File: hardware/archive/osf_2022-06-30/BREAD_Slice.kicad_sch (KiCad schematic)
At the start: 40 parts, among them J1 Conn_01x10_Female, J2 Term_2, J3 Term_2, J4 Term_2, J5 Term_2, J6 Term_2, J7 Term_2, J8 Term_2, K1 G5Q-1, Q1 STGP7NC60HD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

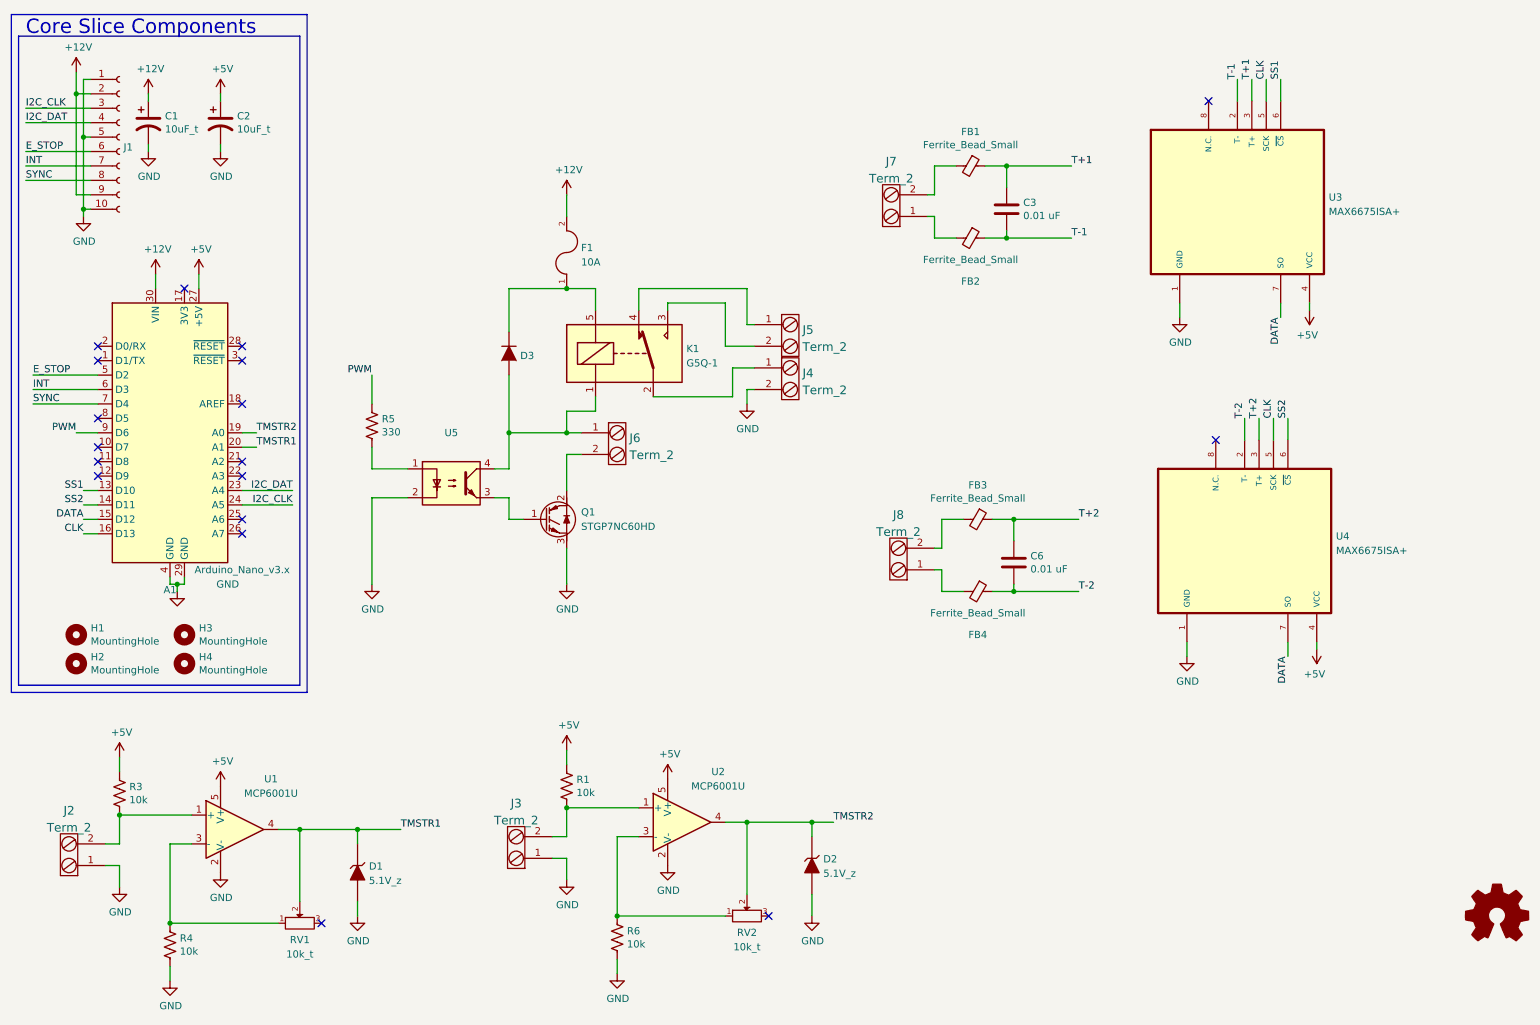
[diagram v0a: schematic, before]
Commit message: added historical scripts and new revisions
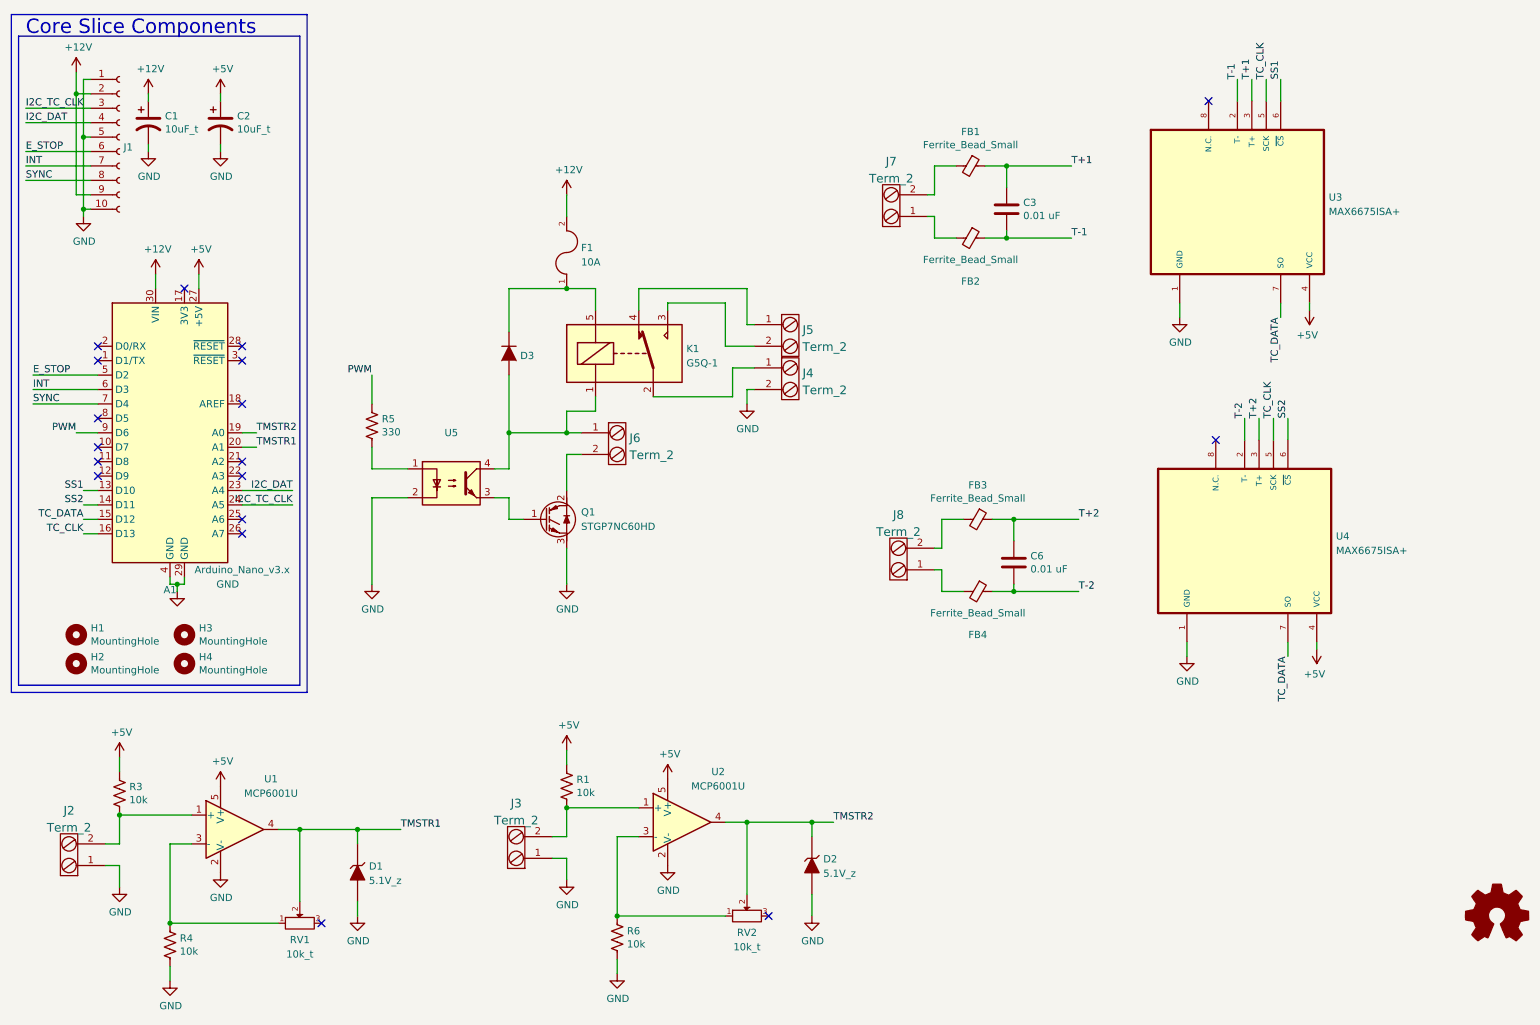
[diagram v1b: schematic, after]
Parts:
- A1: TC_DATAsheet (none) -> http://www.mouser.com/pdfdocs/Gravitech_Arduino_Nano3_0.pdf
- C1, C2: TC_DATAsheet (none) -> https://www.digikey.com/short/qcd8n7
- D1, D2: TC_DATAsheet (none) -> https://www.digikey.com/short/q75wjm
- D3: TC_DATAsheet (none) -> https://www.digikey.com/short/q75wqm
- F1: TC_DATAsheet (none) -> https://www.digikey.com/short/q7wbwz
- J2, J3, J4, J5, J6, J7, J8: TC_DATAsheet (none) -> https://www.digikey.com/short/q7wbhd
- K1: TC_DATAsheet (none) -> https://www.omron.com/ecb/products/pdf/en-g5q.pdf
- Q1: TC_DATAsheet (none) -> http://www.farnell.com/TC_DATAsheets/2309889.pdf
- RV1, RV2: TC_DATAsheet (none) -> https://www.digikey.com/short/qt5j3q
- U1, U2: TC_DATAsheet (none) -> http://ww1.microchip.com/downloads/en/DeviceDoc/21733j.pdf
- U5: TC_DATAsheet (none) -> http://www.vishay.com/docs/83510/tcmt1100.pdf
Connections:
- net CLK renamed TC_CLK
- net DATA renamed TC_DATA
- net I2C_CLK renamed I2C_TC_CLK
